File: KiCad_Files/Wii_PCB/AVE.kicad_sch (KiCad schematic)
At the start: 18 parts

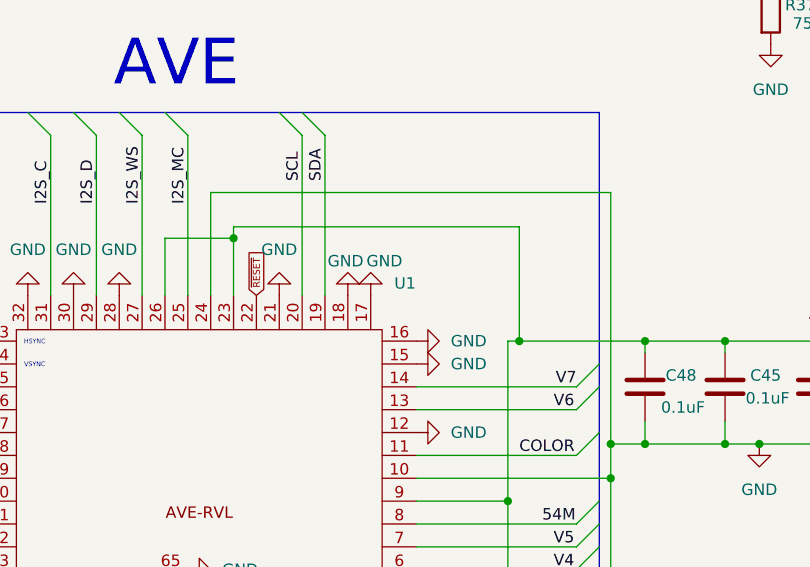
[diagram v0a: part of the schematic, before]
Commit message: Updated RAM & GPU bus to allow custom net rules for measuring intra-track spacing, added pad for reset, removed debug pads, reorganized ram schematic to cluster length matched signals, changed MX chip and U10 symbols, and re-labeled the wifi net interface.
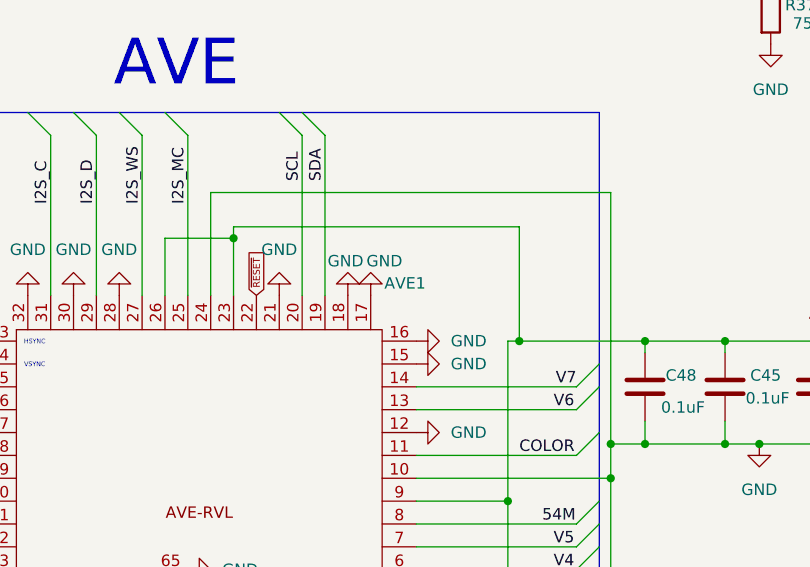
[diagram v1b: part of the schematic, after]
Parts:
- renumbered U1 to AVE1
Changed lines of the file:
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@@
 		(dnp no)
 		(fields_autoplaced yes)
-		(property "Reference" "U1"
+		(property "Reference" "AVE1"
 			(at 146.05 91.3698 0)
 			(effects
@@
 			(project "Wii PCB"
 				(path "/07becb85-5b32-497c-802d-66c73e9db46a/d79f3b7d-4197-4e02-ad8d-484cbd5334e4"
-					(reference "U1")
+					(reference "AVE1")
 					(unit 1)
 				)
